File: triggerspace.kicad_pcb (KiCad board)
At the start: 2 copper layers, 257.6 x 128.5 mm, 171 parts, among them J1 Conn_01x2, J10 Conn_01x12, J11 Conn_01x12, J12 Conn_02x05_Odd_Even, J13 Conn_01x10, J14 Conn_01x10, J15 Conn_01x10, J2 Conn_01x2, J3 Conn_01x4, J4 Conn_01x4, J5 Conn_01x3, J6 Conn_01x3, J7 Conn_01x10, J8 Conn_01x3, J9 Conn_01x2, Q1 2N3904, Q2 2N3904, U1 MCP6002_1, U2 MCP6002_1, U3 MCP6002_1, U4 L7805, U5 LM4040LP-5, U6 74HC595, U8 HCPL-2630, U9 HCPL-0630, X1 CV_X, Y1 CV_Y

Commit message: D8: optional 5.1V zener footprint as an alternative to U5 (LM4040LP-5)
Upright DO-35 footprint inside U5's outline, cathode to GND, anode on the
-5V ref_5 rail; ref_5 re-routed locally around it. README build option and
CHANGELOG entry.
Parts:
- added D8: 5.1V, Diode_THT:D_DO-35_SOD27_P2.54mm_Vertical_KathodeUp, F.Cu at (143.2, 78.7)
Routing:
- net ref_5: track 128.5 -> 126.4 mm
- net GND: track 147.7 -> 149.7 mm
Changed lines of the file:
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@@
 		(tags "CP Radial series Radial pin pitch 2.50mm  diameter 5mm Electrolytic Capacitor")
 		(property "Reference" "C15"
-			(at -2.54 -1.27 180)
+			(at 1.02 3.47 90)
 			(layer "F.SilkS")
 			(effects
@@
 		(embedded_fonts no)
 	)
+	(footprint "Diode_THT:D_DO-35_SOD27_P2.54mm_Vertical_KathodeUp"
+		(layer "F.Cu")
+		(at 143.23 78.73)
+		(descr "Diode, DO-35_SOD27 series, Axial, Vertical, pin pitch=2.54mm, length*diameter=4*2mm^2, http://www.diodes.com/_files/packages/DO-35.pdf")
+		(tags "Diode DO-35_SOD27 series Axial Vertical pin pitch 2.54mm  length 4mm diameter 2mm")
+		(property "Reference" "D8"
+			(at 1.27 -1.78 0)
+			(layer "F.SilkS")
+			(effects
+				(font
+					(size 0.8 0.8)
+					(thickness 0.12)
+				)
+			)
+		)
+		(property "Value" "5.1V"
+			(at 1.27 3.215371 0)
+			(layer "F.Fab")
+			(effects
+				(font
+					(size 1 1)
+					(thickness 0.15)
+				)
+			)
+		)
+		(property "Datasheet" ""
+			(at 0 0 0)
+			(layer "F.Fab")
+			(hide yes)
+			(effects
+				(font
+					(size 1.27 1.27)
+					(thickness 0.15)
+				)
+			)
+		)
+		(property "Description" ""
+			(at 0 0 0)
+			(layer "F.Fab")
+			(hide yes)
+			(effects
+				(font
+					(size 1.27 1.27)
+					(thickness 0.15)
+				)
+			)
+		)
+		(sheetname "/")
+		(sheetfile "triggerspace.kicad_sch")
+		(attr through_hole dnp)
+		(fp_line
+			(start 1.213629 0)
+			(end 1.1 0)
+			(stroke
+				(width 0.12)
+				(type solid)
+			)
+			(layer "F.SilkS")
+		)
+		(fp_circle
+			(center 2.54 0)
+			(end 3.866371 0)
+			(stroke
+				(width 0.12)
+				(type solid)
+			)
+			(fill no)
+			(layer "F.SilkS")
+		)
+		(fp_rect
+			(start -1.05 -1.25)
+			(end 3.79 1.25)
+			(stroke
+				(width 0.05)
+				(type solid)
+			)
+			(fill no)
+			(layer "F.CrtYd")
+		)
+		(fp_line
+			(start 0 0)
+			(end 2.54 0)
+			(stroke
+				(width 0.1)
+				(type solid)
+			)
+			(layer "F.Fab")
+		)
+		(fp_circle
+			(center 2.54 0)
+			(end 3.54 0)
+			(stroke
+				(width 0.1)
+				(type solid)
+			)
+			(fill no)
+			(layer "F.Fab")
+		)
+		(fp_text user "K"
+			(at -1.8 0 0)
+			(layer "F.SilkS")
+			(effects
+				(font
+					(size 1 1)
+					(thickness 0.15)
+				)
+			)
+		)
+		(fp_text user "${REFERENCE}"
+			(at 1.27 -2.326371 0)
+			(layer "F.Fab")
+			(effects
+				(font
+					(size 1 1)
+					(thickness 0.15)
+				)
+			)
+		)
+		(fp_text user "K"
+			(at -1.8 0 0)
+			(layer "F.Fab")
+			(effects
+				(font
+					(size 1 1)
+					(thickness 0.15)
+				)
+			)
+		)
+		(pad "1" thru_hole roundrect
+			(at 0 0)
+			(size 1.6 1.6)
+			(drill 0.8)
+			(layers "*.Cu" "*.Mask")
+			(remove_unused_layers no)
+			(roundrect_rratio 0.15625)
+			(net 3 "GND")
+		)
+		(pad "2" thru_hole circle
+			(at 2.54 0)
+			(size 1.6 1.6)
+			(drill 0.8)
+			(layers "*.Cu" "*.Mask")
+			(remove_unused_layers no)
+			(net 23 "ref_5")
+		)
+		(embedded_fonts no)
+		(model "${KICAD9_3DMODEL_DIR}/Diode_THT.3dshapes/D_DO-35_SOD27_P2.54mm_Vertical_KathodeUp.step"
+			(offset
+				(xyz 0 0 0)
+			)
+			(scale
+				(xyz 1 1 1)
+			)
+			(rotate
+				(xyz 0 0 0)
+			)
+		)
+	)
 	(footprint "MountingHole:MountingHole_3mm"
 		(locked yes)
@@
 		(net 3)
 	)
+	(segment
+		(start 143.9 79.4)
+		(end 145.3 80.8)
+		(width 0.25)
+		(layer "F.Cu")
+		(net 3)
+	)
 	(via
 		(at 162.46 84)
@@
 	)
 	(segment
+		(start 146.5 78.6)
+		(end 147.7 78.6)
+		(width 0.25)
+		(layer "F.Cu")
+		(net 23)
+	)
+	(segment
 		(start 162.56 72.859002)
 		(end 156.679002 78.74)
@@
 	)
 	(segment
+		(start 143.4 79.9)
+		(end 144.1 79.9)
+		(width 0.25)
+		(layer "B.Cu")
+		(net 23)
+	)
+	(segment
 		(start 111.76 89.889949)
 		(end 113.065052 91.195001)
@@
 	)
 	(segment
-		(start 142.02 81.28)
-		(end 144.56 78.74)
-		(width 0.25)
-		(locked yes)
-		(layer "B.Cu")
-		(net 23)
-	)
-	(segment
 		(start 156.679002 78.74)
 		(end 148.318021 78.74)
@@
 	)
 	(segment
-		(start 144.56 78.74)
-		(end 148.298521 78.74)
-		(width 0.25)
-		(locked yes)
-		(layer "B.Cu")
-		(net 23)
-	)
-	(segment
 		(start 135.850047 83.859953)
 		(end 138.43 81.28)
@@
 	)
 	(segment
+		(start 142 81.3)
+		(end 143.4 79.9)
+		(width 0.25)
+		(layer "B.Cu")
+		(net 23)
+	)
+	(segment
+		(start 144.7 79.4)
+		(end 145.1 79)
+		(width 0.25)
+		(layer "B.Cu")
+		(net 23)
+	)
+	(segment
 		(start 135.889527 84.983104)
 		(end 135.889527 90.170473)
@@
 		(layer "B.Cu")
 		(net 23)
+	)
+	(segment
+		(start 144.1 79.9)
+		(end 144.6 79.4)
+		(width 0.25)
+		(layer "B.Cu")
+		(net 23)
+	)
+	(segment
+		(start 144.6 79.4)
+		(end 144.7 79.4)
+		(width 0.25)
+		(layer "B.Cu")
+		(net 23)

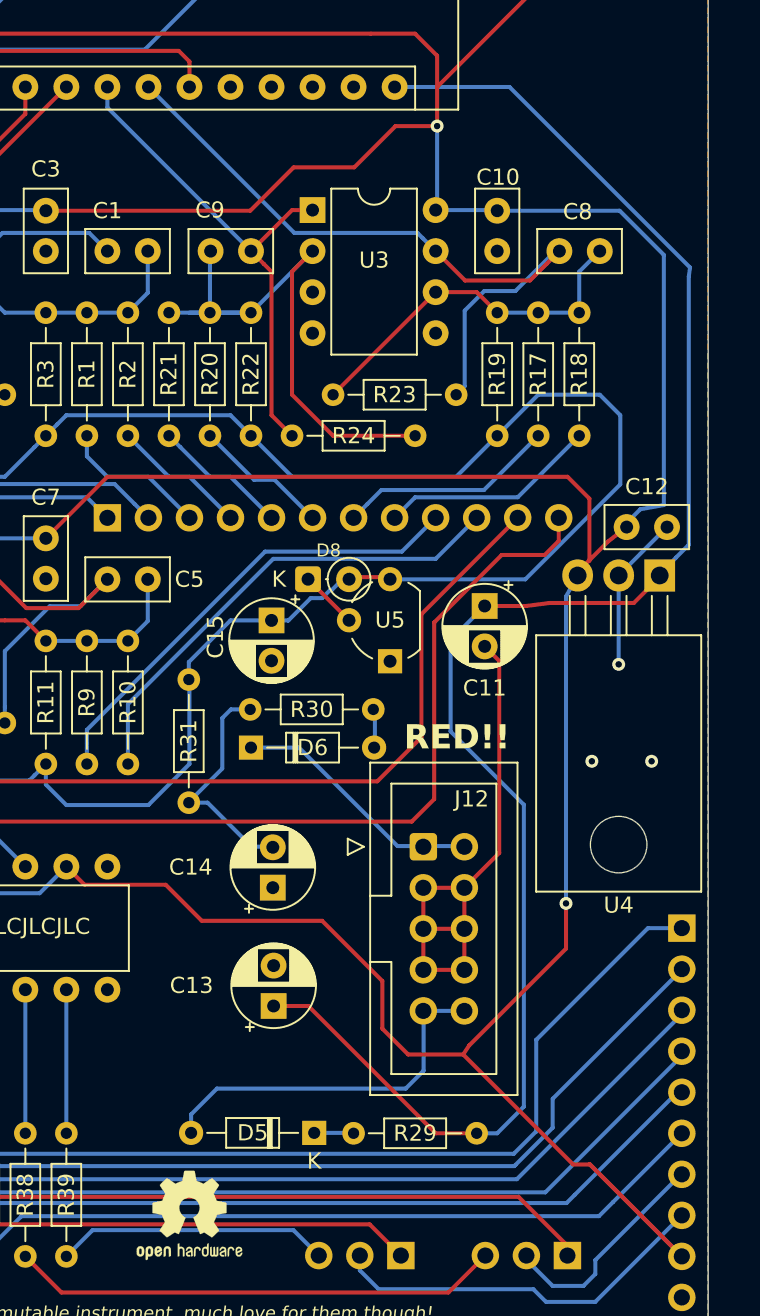
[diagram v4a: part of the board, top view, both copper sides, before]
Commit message: +5V supply options: JP5 (Nano regulator), JP6 (Eurorack +5V), 16-pin J12
- JP5 (open) links the Nano's 5V pin (A1 pin 27) to the +5V rail
- J12 becomes a 2x8 footprint (a 2x5 header still fits pins 1-10); pins 11/12
  (Eurorack +5V) reach the +5V rail through JP6 (open), pins 13-16 unconnected
- U4, C11, C12 marked OPTIONAL on the silkscreen
- D5 moved left, R29 upright (2.54mm), power tracks around J12 re-routed;
  zones refilled with the project's rules
- README: +5V supply build option, JP5/JP6 in Jumpers, updated back PCB diagram;
  CHANGELOG entries
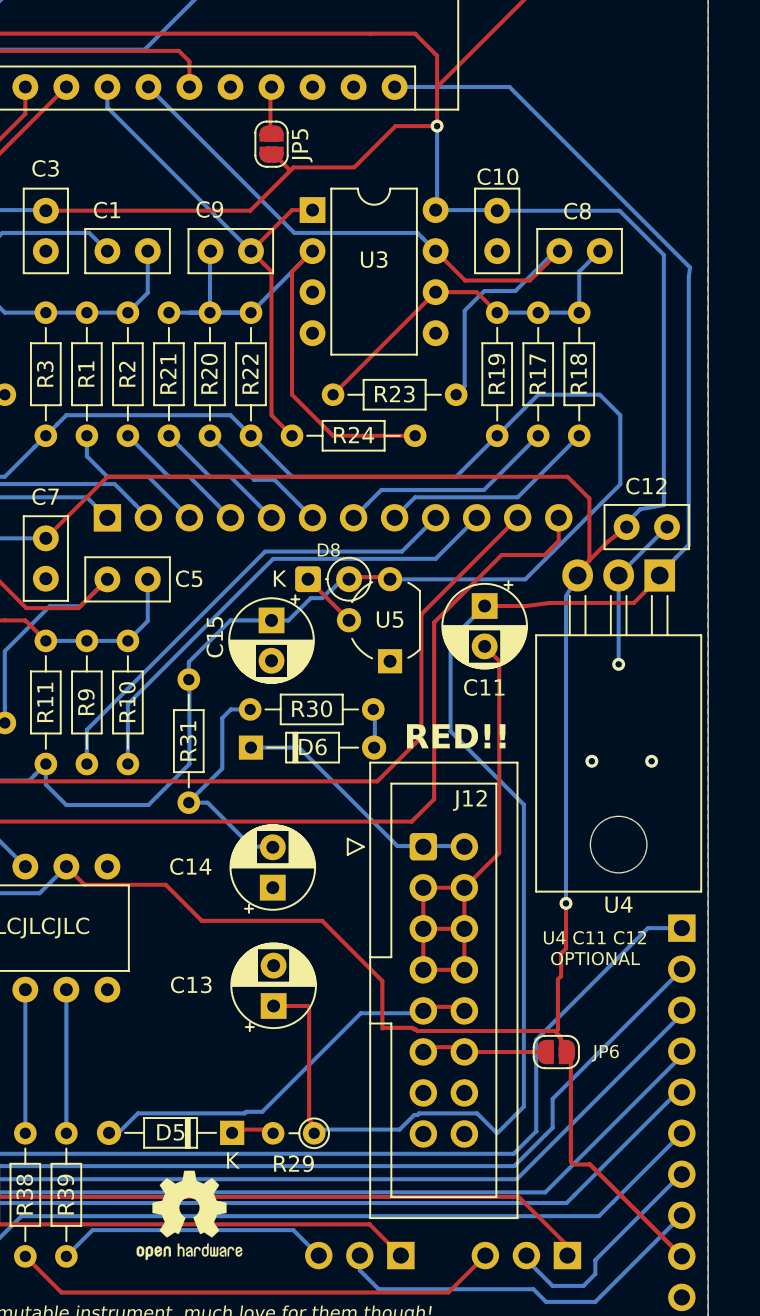
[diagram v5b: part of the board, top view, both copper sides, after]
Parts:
- added JP5: SolderJumper_2_Open, Jumper:SolderJumper-2_P1.3mm_Open_RoundedPad1.0x1.5mm, F.Cu at (141.0, 51.8)
- added JP6: SolderJumper_2_Open, Jumper:SolderJumper-2_P1.3mm_Open_RoundedPad1.0x1.5mm, F.Cu at (158.6, 108.0)
- J12: value Conn_02x05_Odd_Even -> Eurorack power 2x8 (or 2x5); footprint Connector_IDC:IDC-Header_2x05_P2.54mm_Vertical -> Connector_IDC:IDC-Header_2x08_P2.54mm_Vertical
- R29: footprint Resistor_THT:R_Axial_DIN0204_L3.6mm_D1.6mm_P7.62mm_Horizontal -> Resistor_THT:R_Axial_DIN0204_L3.6mm_D1.6mm_P2.54mm_Vertical
- moved R29 10.1 mm to (143.6, 113.0)
- moved D5 5.08 mm to (138.5, 113.0)
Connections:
- A1 pad 27: unconnected-(A1-+5V-Pad27) -> /NANO_5V
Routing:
- net /EURO_5V: track 0.00 -> 4.90 mm
- net +12V: track 107.5 -> 111.4 mm
- net /NANO_5V: track 0.00 -> 1.70 mm
- net Net-(D5-K): track 2.45 -> 1.30 mm
- net Net-(D5-A): track 22.9 -> 22.1 mm
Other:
- board text added: "U4 C11 C12 OPTIONAL"
